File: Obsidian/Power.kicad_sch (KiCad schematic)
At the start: 80 parts, among them J10 Barrel_Jack_Switch, J16 Conn_01x04, Q4 DMP3013SFV, U10 TPSM863257RDXR, U11 TPSM863257RDXR, U18 TLV77325PDBVR, U20 RT9045AGSP / AP2303, U23 NCV59801CML120TCG, U24 SN74LVC1G07DBV, U25 SN74LVC1G07DBV, U4 TPSM863257RDXR, U5 TPSM863257RDXR, U6 TPSM863257RDXR

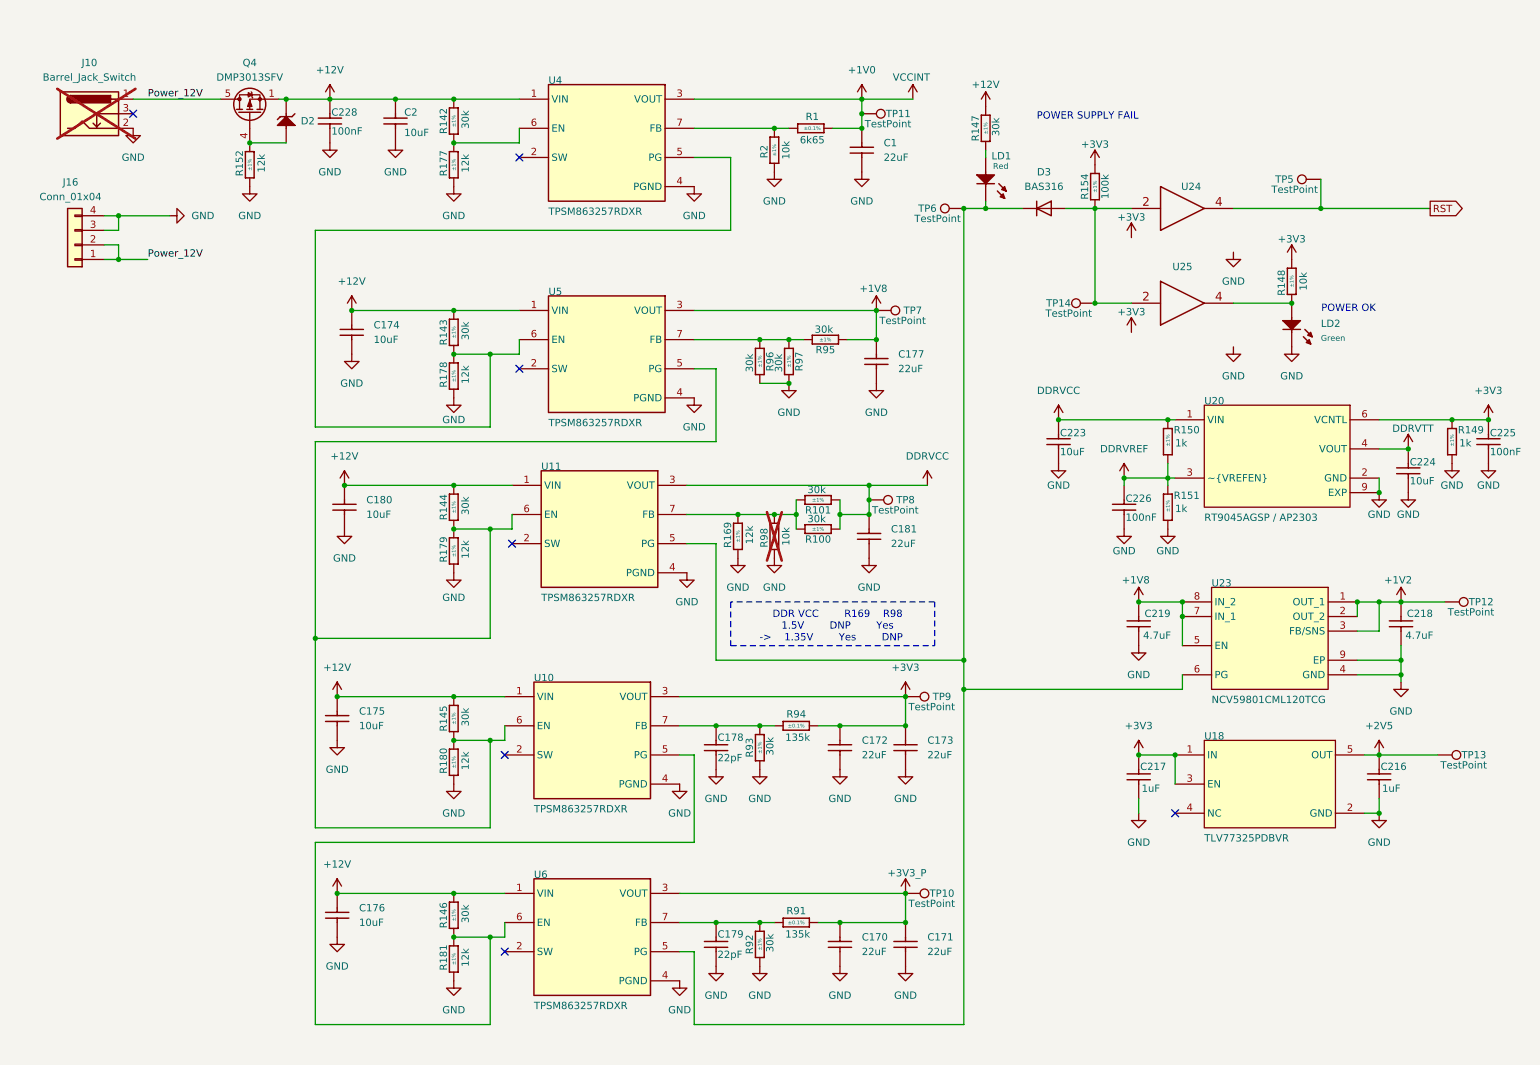
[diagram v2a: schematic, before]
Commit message: Adding symbol library
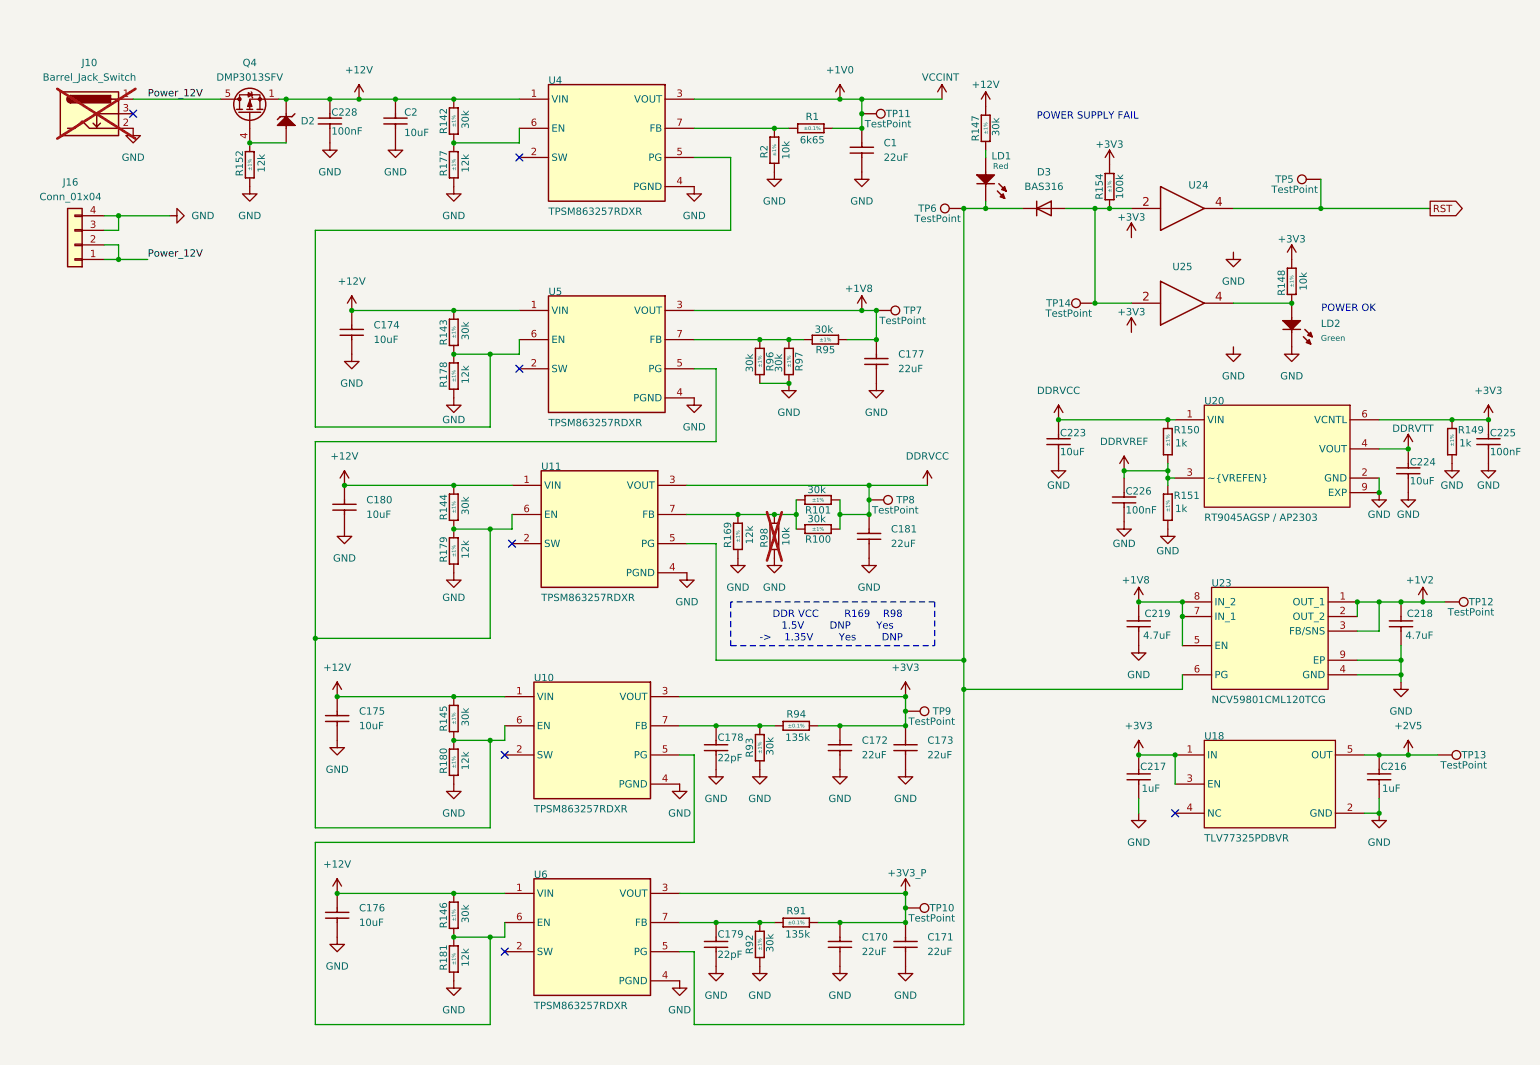
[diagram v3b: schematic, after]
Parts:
- C1, C170, C171, C172, C173, C177, C181: symbol Capacitors SMD:CC0805_22UF_16V_10%_X5R -> Library_Symbol:CC0805_22UF_16V_10%_X5R
- C174, C175, C176, C180, C2: symbol Capacitors SMD:CC0805_10UF_25V_10%_X5R -> Library_Symbol:CC0805_10UF_25V_10%_X5R
- C178, C179: symbol Capacitors SMD:CC0402_22PF_50V_5%_C0G -> Library_Symbol:CC0402_22PF_50V_5%_C0G
- C216, C217: symbol Capacitors SMD:CC0402_1UF_16V_10%_X5R -> Library_Symbol:CC0402_1UF_16V_10%_X5R
- C218, C219: symbol Capacitors SMD:CC0402_4.7UF_16V_20%_X5R -> Library_Symbol:CC0402_4.7UF_16V_20%_X5R
- C223, C224: symbol Capacitors SMD:CC0402_10UF_6.3V_20%_X5R -> Library_Symbol:CC0402_10UF_6.3V_20%_X5R
- C225, C226, C228: symbol Capacitors SMD:CC0402_100NF_50V_10%_X7R -> Library_Symbol:CC0402_100NF_50V_10%_X7R
- D2: symbol Diodes:MM3Z12VB -> Library_Symbol:MM3Z12VB
- D3: symbol Diode:BAS316 -> Library_Symbol:BAS316
- J10: symbol Connector:Barrel_Jack_Switch -> Library_Symbol:Barrel_Jack_Switch
- J16: symbol Connector_Generic:Conn_01x04 -> Library_Symbol:Conn_01x04
- LD1: symbol LEDs & Displays:LED_OSRAM_LS_Q976-NR-1 -> Library_Symbol:LED_OSRAM_LS_Q976-NR-1
- LD2: symbol LEDs & Displays:LED_KINGBRIGHT_KPH-1608CGCK -> Library_Symbol:LED_KINGBRIGHT_KPH-1608CGCK
- Q4: symbol Transistor_FET:DMP3013SFV -> Library_Symbol:DMP3013SFV
- R1: symbol Resistors SMD:R0603_6K65_0.1%_0.063W_10PPM -> Library_Symbol:R0603_6K65_0.1%_0.063W_10PPM
- R100, R101, R142, R143, R144, R145, R146, R147, R92, R93, R95, R96, R97: symbol Resistors SMD:R0402_30K_1%_0.0625W_100PPM -> Library_Symbol:R0402_30K_1%_0.0625W_100PPM
- R148, R2, R98: symbol Resistors SMD:R0402_10K_1%_0.0625W_100PPM -> Library_Symbol:R0402_10K_1%_0.0625W_100PPM
- R149, R150, R151: symbol Resistors SMD:R0402_1K_1%_0.0625W_100PPM -> Library_Symbol:R0402_1K_1%_0.0625W_100PPM
- R152, R169, R177, R178, R179, R180, R181: symbol Resistors SMD:R0402_12K_1%_0.0625W_100PPM -> Library_Symbol:R0402_12K_1%_0.0625W_100PPM
- R154: symbol Resistors SMD:R0402_100K_1%_0.0625W_100PPM -> Library_Symbol:R0402_100K_1%_0.0625W_100PPM
- R91, R94: symbol Resistors SMD:R0805_135K_0.1%_0.1W_25PPM_KOA_RN73R2ATTD1353B25 -> Library_Symbol:R0805_135K_0.1%_0.1W_25PPM_KOA_RN73R2ATTD1353B25
- TP10, TP11, TP12, TP13, TP14, TP5, TP6, TP7, TP8, TP9: symbol Connector:TestPoint -> Library_Symbol:TestPoint
- U10: symbol Sheet2-altium-import:root_0_TPSM863257RDXR -> Library_Symbol:root_0_TPSM863257RDXR_4
- U11: symbol Sheet2-altium-import:root_0_TPSM863257RDXR -> Library_Symbol:root_0_TPSM863257RDXR_3
- U18: symbol Sheet3-altium-import:root_0_9444cdc507fe29f20f0adc9980b4e13 -> Library_Symbol:root_0_9444cdc507fe29f20f0adc9980b4e13
- U20: symbol Sheet3-altium-import:root_0_AP2303MPTR-G1 -> Library_Symbol:root_0_AP2303MPTR-G1
- U23: symbol Sheet3-altium-import:root_0_NCV59801CML120TCG -> Library_Symbol:root_0_NCV59801CML120TCG
- U24: symbol Standard Logic:SN74LVC1G07DBV -> Library_Symbol:SN74LVC1G07DBV_1
- U25: symbol Standard Logic:SN74LVC1G07DBV -> Library_Symbol:SN74LVC1G07DBV
- U4: symbol Sheet2-altium-import:root_0_TPSM863257RDXR -> Library_Symbol:root_0_TPSM863257RDXR_1
- U5: symbol Sheet2-altium-import:root_0_TPSM863257RDXR -> Library_Symbol:root_0_TPSM863257RDXR_2
- U6: symbol Sheet2-altium-import:root_0_TPSM863257RDXR -> Library_Symbol:root_0_TPSM863257RDXR
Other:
- moved on the sheet: C226, R154, TP10, TP9

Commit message: Correct Schematic errors
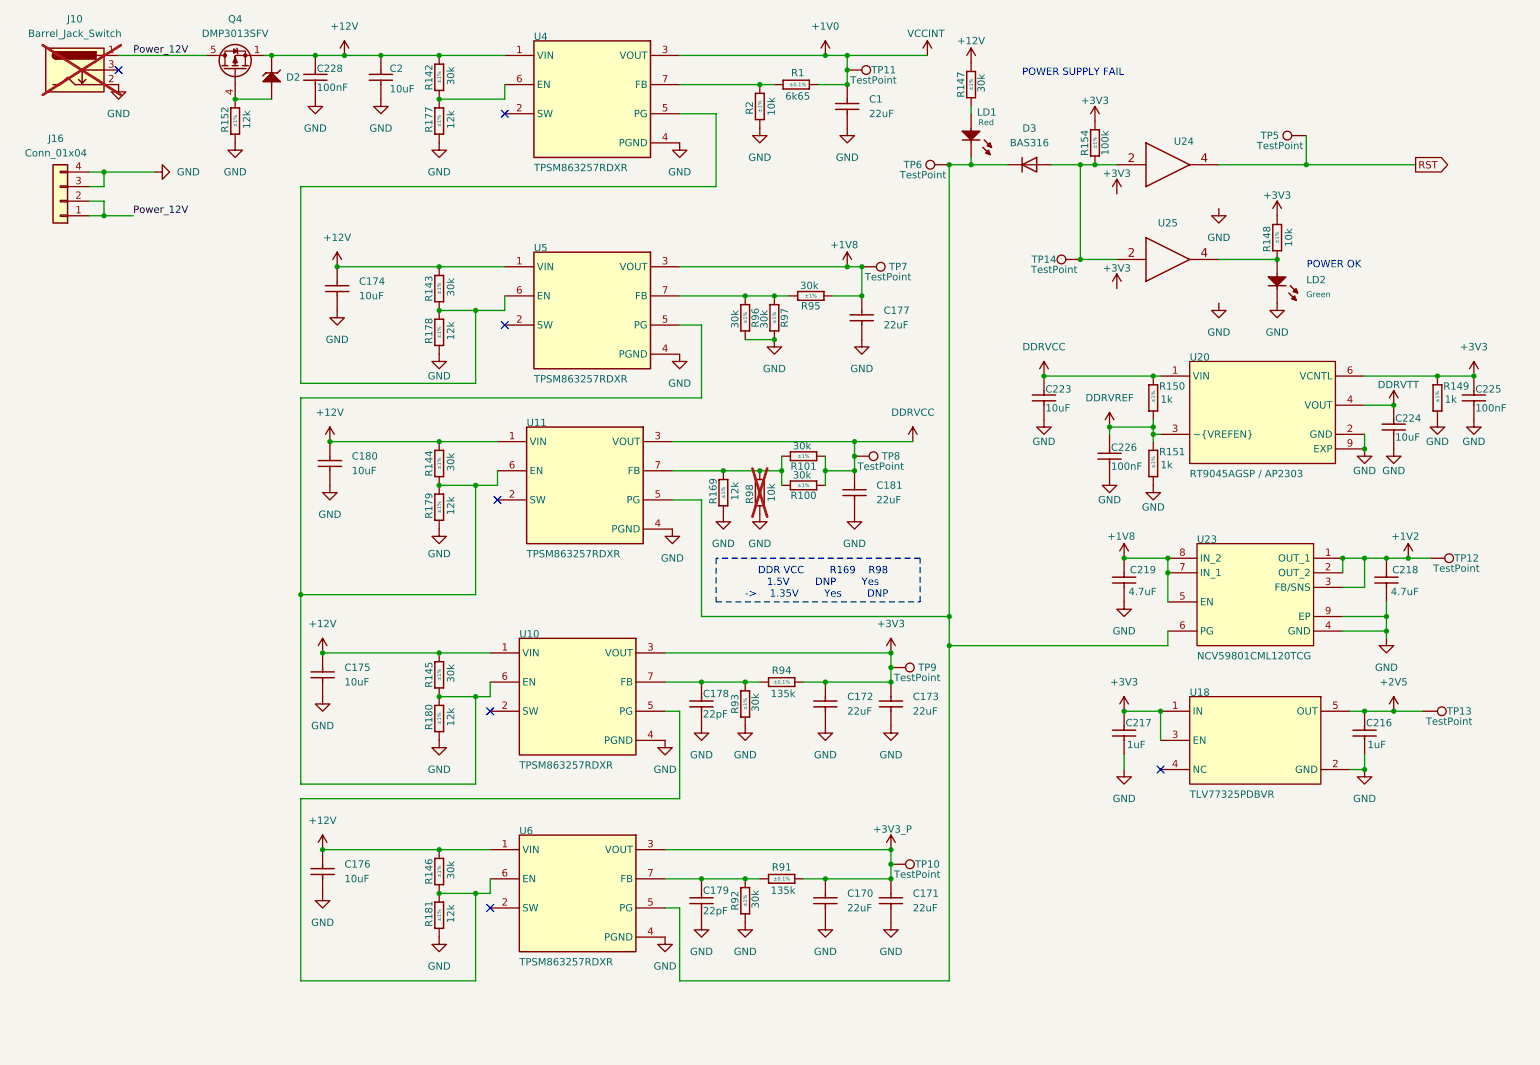
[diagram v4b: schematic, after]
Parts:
- C1, C170, C171, C172, C173, C177, C181: footprint Capacitors SMD:CAPC2012X135N -> Footprint:CAPC2012X135N
- C174, C175, C176, C180, C2: footprint Capacitors SMD:CAPC2012X95N -> Footprint:CAPC2012X95N
- C178, C179, C216, C217, C218, C219, C225, C226, C228: footprint Capacitors SMD:CAPC1005X55N -> Footprint:CAPC1005X55N
- C223, C224: footprint Capacitors SMD:CAPC1005X70N -> Footprint:CAPC1005X70N
- D2: footprint ICs And Semiconductors SMD:SODFL2513X100N -> Footprint:SODFL2513X100N
- D3: footprint Diode_SMD:D_SOD-323 -> Footprint:D_SOD-323
- J10: footprint Connector_BarrelJack:BarrelJack_GCT_DCJ200-10-A_Horizontal -> Footprint:BarrelJack_GCT_DCJ200-10-A_Horizontal
- J16: JLC_3DModel_Q (none) -> 3a9589fe0d364ed5b6653693e78db6f8; JLC_3D_Size (none) -> 22.4 19.2
- LD1: footprint ICs And Semiconductors SMD:LED_OSRAM_LS Q976 -> Footprint:LED_OSRAM_LS Q976
- LD2: footprint ICs And Semiconductors SMD:LED_KINGBRIGHT_KPH-1608CGCK -> Footprint:LED_KINGBRIGHT_KPH-1608CGCK
- Q4: footprint Package_SON:Diodes_PowerDI3333-8 -> Footprint:Diodes_PowerDI3333-8
- R1: footprint Resistors SMD:RESC1608X55N -> Footprint:RESC1608X55N
- R100, R101, R142, R143, R144, R145, R146, R147, R148, R149, R150, R151, R152, R154, R169, R177, R178, R179, R180, R181, R2, R92, R93, R95, R96, R97, R98: footprint Resistors SMD:RESC1005X40N -> Footprint:RESC1005X40N
- R91, R94: footprint Resistors SMD:RESC2012X60N -> Footprint:RESC2012X60N
- U10, U11, U4, U5, U6: footprint VREG_TPSM863257RDXR -> Footprint:VREG_TPSM863257RDXR
- U18: footprint Package_TO_SOT_SMD:SOT-23-5 -> Footprint:SOT-23-5
- U20: footprint ICs And Semiconductors SMD:SOIC127P600X168-9N-S230 -> Footprint:SOIC127P600X168-9N-S230
- U23: footprint ICs And Semiconductors SMD:SON65P300X300X100-9N-R170X245 -> Footprint:SON65P300X300X100-9N-R170X245
- U24, U25: footprint ICs And Semiconductors SMD:SOT95P280X145-5N -> Footprint:SOT95P280X145-5N
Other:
- moved on the sheet: C1, C170, C171, C172, C173, C174, C175, C176, C177, C178, C179, C180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

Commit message: adding 3D files, 3D model of twist, and correct DRC
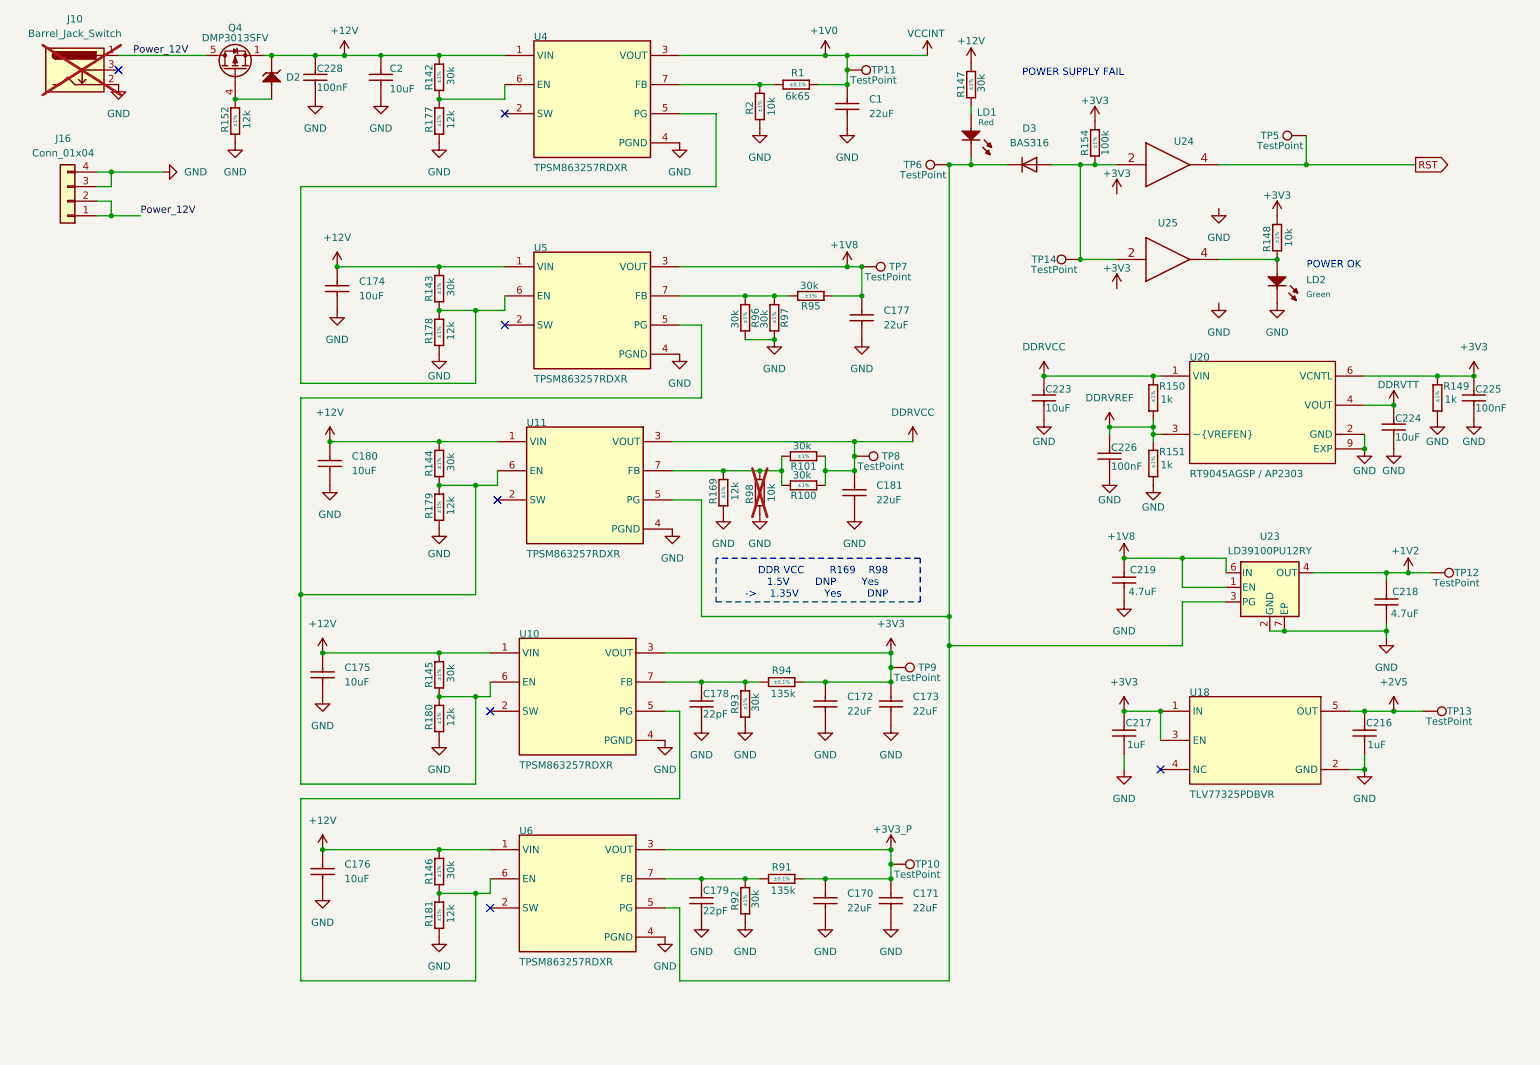
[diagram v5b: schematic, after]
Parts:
- removed U23: NCV59801CML120TCG, Footprint:SON65P300X300X100-9N-R170X245, symbol Library_Symbol:root_0_NCV59801CML120TCG
- added U23: LD39100PU12RY, Package_DFN_QFN:DFN-6-1EP_3x3mm_P0.95mm_EP1.7x2.6mm, symbol Library_Symbol:LD39100PU12RY_DFN6
- C178, C179, C216, C217, C218, C219, C225, C226, C228: footprint Footprint:CAPC1005X55N -> Capacitor_SMD:C_0402_1005Metric
- R1: value R0603_6K65_0.1%_0.063W_10PPM -> R0603_6K65_0.1%_0.060W_10PPM; footprint Footprint:RESC1608X55N -> Footprint:RESC1005X40N; Case 0603 -> 0402; LCSC (none) -> C2692937; Manufacturer Part Number R0603_6K65_0.1%_0.063W_10PPM -> R0603_6K65_0.1%_0.060W_10PPM; Part Number R0603_6K65_0.1%_0.063W_10PPM -> R0603_6K65_0.1%_0.060W_10PPM; Power 0.063W -> 0.060W
- R94: footprint Footprint:RESC2012X60N -> Footprint:RESC1608X55N; Case 0805 -> 0603
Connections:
- net +1V2: now also U23.4 (OUT)
- net +1V8: now also U23.1 (EN), U23.6 (IN)
- net GND: now also U23.2 (GND), U23.7 (EP)
- net at D3.1 (K), LD1.1 (C), TP6.1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: now also U23.3 (PG)
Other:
- moved on the sheet: C218, J16, TP12

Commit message: correcting some footprint issues
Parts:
- R1: value R0603_6K65_0.1%_0.060W_10PPM -> R0402_6K65_0.1%_0.060W_10PPM
- R91: value R0805_135K_0.1%_0.1W_25PPM_KOA_RN73R2ATTD1353B25 -> R0603_135K_0.1%_0.1W_25PPM_KOA_RN73R2ATTD1353B25; footprint Footprint:RESC2012X60N -> Footprint:RESC1608X55N
- R94: value R0805_135K_0.1%_0.1W_25PPM_KOA_RN73R2ATTD1353B25 -> R0603_135K_0.1%_0.1W_25PPM_KOA_RN73R2ATTD1353B25
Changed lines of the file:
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@@
 			)
 		)
-		(property "Value" "R0805_135K_0.1%_0.1W_25PPM_KOA_RN73R2ATTD1353B25"
+		(property "Value" "R0603_135K_0.1%_0.1W_25PPM_KOA_RN73R2ATTD1353B25"
 			(at 147.32 156.337 0)
 			(effects
@@
 			)
 		)
-		(property "Footprint" "Footprint:RESC2012X60N"
+		(property "Footprint" "Footprint:RESC1608X55N"
 			(at 147.32 154.432 0)
 			(effects
@@
 			)
 		)
-		(property "Value" "R0603_6K65_0.1%_0.060W_10PPM"
+		(property "Value" "R0402_6K65_0.1%_0.060W_10PPM"
 			(at 142.24 27.813 0)
 			(effects
@@
 			)
 		)
-		(property "Value" "R0805_135K_0.1%_0.1W_25PPM_KOA_RN73R2ATTD1353B25"
+		(property "Value" "R0603_135K_0.1%_0.1W_25PPM_KOA_RN73R2ATTD1353B25"
 			(at 147.32 122.047 0)
 			(effects
